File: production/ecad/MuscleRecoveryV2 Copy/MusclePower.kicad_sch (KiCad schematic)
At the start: 23 parts, among them IC1 LC709203FQH-01TWG, Q1 FDN340P, U1 AP1117-33, U2 MCP73831-2-OT

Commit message: Created New Layout
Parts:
- C15, C16, C17, C18, C5: footprint Capacitor_SMD:C_0805_2012Metric -> Capacitor_SMD:C_0402_1005Metric
- D1: footprint LED_THT:LED_D1.8mm_W3.3mm_H2.4mm -> Inductor_SMD:L_01005_0402Metric
- D3, D4: footprint LED_THT:LED_D1.8mm_W3.3mm_H2.4mm -> LED_SMD:LED_0402_1005Metric
- R32, R33, R36, R37, R38, R39: footprint Resistor_SMD:R_0805_2012Metric -> Resistor_SMD:R_0402_1005Metric
- R41, R42, R43: footprint Resistor_SMD:R_0805_2012Metric -> Resistor_SMD:R_01005_0402Metric
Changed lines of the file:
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@@
       (effects (font (size 1.27 1.27)) (justify left))
     )
-    (property "Footprint" "Capacitor_SMD:C_0805_2012Metric" (at 132.715 51.435 0)
+    (property "Footprint" "Capacitor_SMD:C_0402_1005Metric" (at 132.715 51.435 0)
       (effects (font (size 1.27 1.27)) hide)
     )
@@
       (effects (font (size 1.27 1.27)))
     )
-    (property "Footprint" "Resistor_SMD:R_0805_2012Metric" (at 149.86 49.53 0)
+    (property "Footprint" "Resistor_SMD:R_0402_1005Metric" (at 149.86 49.53 0)
       (effects (font (size 1.27 1.27)) hide)
     )
@@
       (effects (font (size 1.27 1.27)))
     )
-    (property "Footprint" "Resistor_SMD:R_0805_2012Metric" (at 64.77 114.808 90)
+    (property "Footprint" "Resistor_SMD:R_01005_0402Metric" (at 64.77 114.808 90)
       (effects (font (size 1.27 1.27)) hide)
     )
@@
       (effects (font (size 1.27 1.27)) (justify left))
     )
-    (property "Footprint" "Resistor_SMD:R_0805_2012Metric" (at 96.012 106.68 90)
+    (property "Footprint" "Resistor_SMD:R_0402_1005Metric" (at 96.012 106.68 90)
       (effects (font (size 1.27 1.27)) hide)
     )
@@
       (effects (font (size 1.27 1.27)))
     )
-    (property "Footprint" "Resistor_SMD:R_0805_2012Metric" (at 64.77 117.348 90)
+    (property "Footprint" "Resistor_SMD:R_01005_0402Metric" (at 64.77 117.348 90)
       (effects (font (size 1.27 1.27)) hide)
     )
@@
       (effects (font (size 1.27 1.27)))
     )
-    (property "Footprint" "Resistor_SMD:R_0805_2012Metric" (at 38.608 102.87 90)
+    (property "Footprint" "Resistor_SMD:R_01005_0402Metric" (at 38.608 102.87 90)
       (effects (font (size 1.27 1.27)) hide)
     )
@@
       (effects (font (size 1.27 1.27)))
     )
-    (property "Footprint" "Resistor_SMD:R_0805_2012Metric" (at 149.86 58.42 0)
+    (property "Footprint" "Resistor_SMD:R_0402_1005Metric" (at 149.86 58.42 0)
       (effects (font (size 1.27 1.27)) hide)
     )
@@
       (effects (font (size 1.27 1.27)))
     )
-    (property "Footprint" "LED_THT:LED_D1.8mm_W3.3mm_H2.4mm" (at 159.385 58.42 90)
+    (property "Footprint" "LED_SMD:LED_0402_1005Metric" (at 159.385 58.42 90)
       (effects (font (size 1.27 1.27)) hide)
     )
@@
       (effects (font (size 1.27 1.27)) (justify left))
     )
-    (property "Footprint" "Capacitor_SMD:C_0805_2012Metric" (at 23.8252 111.76 0)
+    (property "Footprint" "Capacitor_SMD:C_0402_1005Metric" (at 23.8252 111.76 0)
       (effects (font (size 1.27 1.27)) hide)
     )
@@
       (effects (font (size 1.27 1.27)) (justify left))
     )
-    (property "Footprint" "Resistor_SMD:R_0805_2012Metric" (at 41.91 118.618 90)
+    (property "Footprint" "Resistor_SMD:R_0402_1005Metric" (at 41.91 118.618 90)
       (effects (font (size 1.27 1.27)) hide)
     )
@@
       (effects (font (size 1.27 1.27)) (justify left))
     )
-    (property "Footprint" "Capacitor_SMD:C_0805_2012Metric" (at 50.8 58.42 0)
+    (property "Footprint" "Capacitor_SMD:C_0402_1005Metric" (at 50.8 58.42 0)
       (effects (font (size 1.27 1.27)) hide)
     )
@@
       (effects (font (size 1.27 1.27)) (justify right))
     )
-    (property "Footprint" "LED_THT:LED_D1.8mm_W3.3mm_H2.4mm" (at 36.83 110.49 0)
+    (property "Footprint" "Inductor_SMD:L_01005_0402Metric" (at 36.83 110.49 0)
       (effects (font (size 1.27 1.27)) hide)
     )
@@
       (effects (font (size 1.27 1.27)) (justify left))
     )
-    (property "Footprint" "Capacitor_SMD:C_0805_2012Metric" (at 95.25 58.42 0)
+    (property "Footprint" "Capacitor_SMD:C_0402_1005Metric" (at 95.25 58.42 0)
       (effects (font (size 1.27 1.27)) hide)
     )
@@
       (effects (font (size 1.27 1.27)) (justify left))
     )
-    (property "Footprint" "Capacitor_SMD:C_0805_2012Metric" (at 202.565 48.895 0)
+    (property "Footprint" "Capacitor_SMD:C_0402_1005Metric" (at 202.565 48.895 0)
       (effects (font (size 1.27 1.27)) hide)
     )
@@
       (effects (font (size 1.27 1.27)))
     )
-    (property "Footprint" "LED_THT:LED_D1.8mm_W3.3mm_H2.4mm" (at 159.385 49.53 90)
+    (property "Footprint" "LED_SMD:LED_0402_1005Metric" (at 159.385 49.53 90)
       (effects (font (size 1.27 1.27)) hide)
     )
@@
       (effects (font (size 1.27 1.27)))
     )
-    (property "Footprint" "Resistor_SMD:R_0805_2012Metric" (at 193.675 52.705 0)
+    (property "Footprint" "Resistor_SMD:R_0402_1005Metric" (at 193.675 52.705 0)
       (effects (font (size 1.27 1.27)) hide)
     )
@@
       (effects (font (size 1.27 1.27)) (justify left))
     )
-    (property "Footprint" "Resistor_SMD:R_0805_2012Metric" (at 27.94 59.69 0)
-      (effects (font (size 1.27 1.27)) hide)
-    )
+    (property "Footprint" "Resistor_SMD:R_0402_1005Metric" (at 27.94 59.69 0)
+      (effects (font (size 1.27 1.27)) hide)
+    )

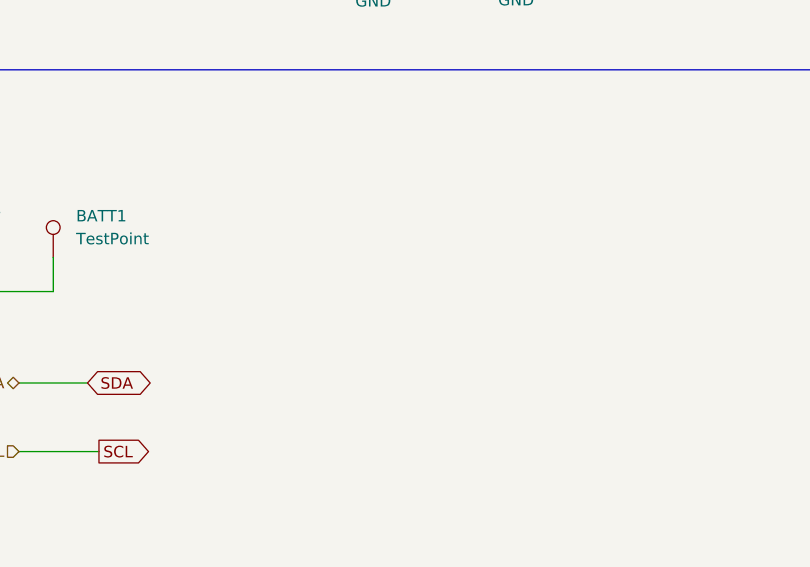
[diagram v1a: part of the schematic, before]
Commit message: Pushing Layout Changes for Andy's Layout
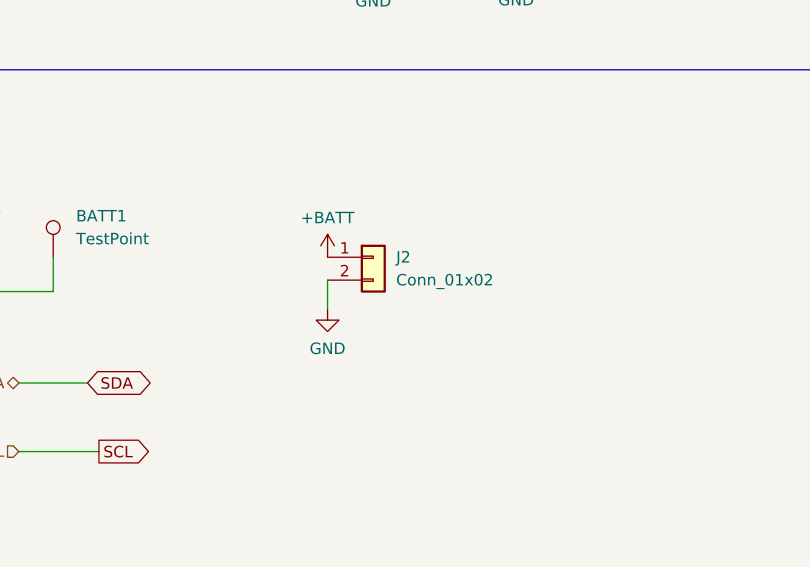
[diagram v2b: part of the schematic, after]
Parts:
- added J2: Conn_01x02, Connector:JWT_A3963_1x02_P3.96mm_Vertical, symbol Connector_Generic:Conn_01x02
- R41, R42, R43: footprint Resistor_SMD:R_01005_0402Metric -> Resistor_SMD:R_0402_1005Metric
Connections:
- net +BATT: now also J2.1 (Pin_1)
- net GND: now also J2.2 (Pin_2)
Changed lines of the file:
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@@
+    (stroke (width 0) (type default))
+  )
+  (wire (pts (xy 172.72 102.87) (xy 172.72 106.045))
     (stroke (width 0) (type default))
   )
@@
       (effects (font (size 1.27 1.27)))
     )
-    (property "Footprint" "Resistor_SMD:R_01005_0402Metric" (at 64.77 114.808 90)
+    (property "Footprint" "Resistor_SMD:R_0402_1005Metric" (at 64.77 114.808 90)
       (effects (font (size 1.27 1.27)) hide)
     )
@@
         (path "/ec7ffed6-1d2d-48f7-b073-d0a7d4b8c858"
           (reference "#PWR026") (unit 1)
+        )
+      )
+    )
+  )
+  (symbol (lib_id "power:+BATT") (at 172.72 100.33 0) (unit 1)
+    (in_bom yes) (on_board yes) (dnp no) (fields_autoplaced)
+    (property "Reference" "#PWR064" (at 172.72 104.14 0)
+      (effects (font (size 1.27 1.27)) hide)
+    )
+    (property "Value" "+BATT" (at 172.72 95.9612 0)
+      (effects (font (size 1.27 1.27)))
+    )
+    (property "Footprint" "" (at 172.72 100.33 0)
+      (effects (font (size 1.27 1.27)) hide)
+    )
+    (property "Datasheet" "" (at 172.72 100.33 0)
+      (effects (font (size 1.27 1.27)) hide)
+    )
+    (pin "1")
+    (instances
+      (project "MuscleRecoveryV1"
+        (path "/4e550305-79d2-4e4a-a502-817ebcc79f9a/648f095b-a230-48ff-8dbf-d0fbef398770"
+          (reference "#PWR064") (unit 1)
+        )
+      )
+      (project "Power For Muscle Recovery"
+        (path "/68ba6acb-d7b0-4091-ad4f-10769cda4f80"
+          (reference "#PWR02") (unit 1)
+        )
+      )
+      (project "New Test"
+        (path "/ec7ffed6-1d2d-48f7-b073-d0a7d4b8c858"
+          (reference "#PWR03") (unit 1)
         )
       )
@@
       (effects (font (size 1.27 1.27)))
     )
-    (property "Footprint" "Resistor_SMD:R_01005_0402Metric" (at 64.77 117.348 90)
+    (property "Footprint" "Resistor_SMD:R_0402_1005Metric" (at 64.77 117.348 90)
       (effects (font (size 1.27 1.27)) hide)
     )
@@
       (effects (font (size 1.27 1.27)))
     )
-    (property "Footprint" "Resistor_SMD:R_01005_0402Metric" (at 38.608 102.87 90)
+    (property "Footprint" "Resistor_SMD:R_0402_1005Metric" (at 38.608 102.87 90)
       (effects (font (size 1.27 1.27)) hide)
     )
@@
     )
   )
+  (symbol (lib_id "power:GND") (at 172.72 106.045 0) (unit 1)
+    (in_bom yes) (on_board yes) (dnp no) (fields_autoplaced)
+    (property "Reference" "#PWR065" (at 172.72 112.395 0)
+      (effects (font (size 1.27 1.27)) hide)
+    )
+    (property "Value" "GND" (at 172.72 110.49 0)
+      (effects (font (size 1.27 1.27)))
+    )
+    (property "Footprint" "" (at 172.72 106.045 0)
+      (effects (font (size 1.27 1.27)) hide)
+    )
+    (property "Datasheet" "" (at 172.72 106.045 0)
+      (effects (font (size 1.27 1.27)) hide)
+    )
+    (pin "1")
+    (instances
+      (project "MuscleRecoveryV1"
+        (path "/4e550305-79d2-4e4a-a502-817ebcc79f9a/648f095b-a230-48ff-8dbf-d0fbef398770"
+          (reference "#PWR065") (unit 1)
+        )
+      )
+    )
+  )
   (symbol (lib_id "Device:LED") (at 36.83 110.49 90) (unit 1)
     (in_bom yes) (on_board yes) (dnp no)
@@
         )
       )
+    )
+  )
+  (symbol (lib_id "Connector_Generic:Conn_01x02") (at 177.8 100.33 0) (unit 1)
+    (in_bom yes) (on_board yes) (dnp no) (fields_autoplaced)
+    (property "Reference" "J2" (at 180.34 100.33 0)
+      (effects (font (size 1.27 1.27)) (justify left))
+    )
+    (property "Value" "Conn_01x02" (at 180.34 102.87 0)
+      (effects (font (size 1.27 1.27)) (justify left))
+    )
+    (property "Footprint" "Connector:JWT_A3963_1x02_P3.96mm_Vertical" (at 177.8 100.33 0)
+      (effects (font (size 1.27 1.27)) hide)
+    )
+    (property "Datasheet" "~" (at 177.8 100.33 0)
+      (effects (font (size 1.27 1.27)) hide)
+    )
+    (pin "1")
+    (pin "2")
+    (instances
+      (project "MuscleRecoveryV1"
+        (path "/4e550305-79d2-4e4a-a502-817ebcc79f9a/648f095b-a230-48ff-8dbf-d0fbef398770"
+          (reference "J2") (unit 1)
+        )
+      )

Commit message: Committing My pliminary placement for my PCB <3
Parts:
- C15, C16: footprint Capacitor_SMD:C_0402_1005Metric -> Capacitor_SMD:C_0805_2012Metric
- R32: footprint Resistor_SMD:R_0402_1005Metric -> Resistor_SMD:R_0805_2012Metric
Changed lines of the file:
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@@
       (effects (font (size 1.27 1.27)) (justify left))
     )
-    (property "Footprint" "Capacitor_SMD:C_0402_1005Metric" (at 50.8 58.42 0)
+    (property "Footprint" "Capacitor_SMD:C_0805_2012Metric" (at 50.8 58.42 0)
       (effects (font (size 1.27 1.27)) hide)
     )
@@
       (effects (font (size 1.27 1.27)) (justify left))
     )
-    (property "Footprint" "Capacitor_SMD:C_0402_1005Metric" (at 95.25 58.42 0)
+    (property "Footprint" "Capacitor_SMD:C_0805_2012Metric" (at 95.25 58.42 0)
       (effects (font (size 1.27 1.27)) hide)
     )
@@
       (effects (font (size 1.27 1.27)) (justify left))
     )
-    (property "Footprint" "Resistor_SMD:R_0402_1005Metric" (at 27.94 59.69 0)
-      (effects (font (size 1.27 1.27)) hide)
-    )
+    (property "Footprint" "Resistor_SMD:R_0805_2012Metric" (at 27.94 59.69 0)
+      (effects (font (size 1.27 1.27)) hide)
+    )

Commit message: committing some recent changes to layout
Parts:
- removed J2: Conn_01x02, Connector:JWT_A3963_1x02_P3.96mm_Vertical, symbol Connector_Generic:Conn_01x02
- added J1: S2B-PH-SM4-TB_LF__SN_, Muscle_Recovery_Footprint_Library:JST_S2B-PH-SM4-TB_LF__SN_, symbol MuscleRecoverySymbolLibray:S2B-PH-SM4-TB_LF__SN_
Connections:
- net +BATT: now also J1.1
- net GND: now also J1.2
- no-connect marks 2 -> 4
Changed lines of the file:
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@@
   (junction (at 50.8 54.0004) (diameter 0) (color 0 0 0 0)
   )
+  (no_connect (at 184.15 104.775))
   (no_connect (at 91.44 118.11))
   (no_connect (at 91.44 120.65))
+  (no_connect (at 184.15 107.315))
   (wire (pts (xy 95.25 49.53) (xy 95.25 51.7144))
     (stroke (width 0) (type default))
@@
     (stroke (width 0) (type default))
   )
+  (wire (pts (xy 184.15 99.695) (xy 175.26 99.695))
+    (stroke (width 0) (type default))
+  )
   (wire (pts (xy 152.4 49.53) (xy 156.845 49.53))
     (stroke (width 0) (type default))
@@
     (stroke (width 0) (type default))
   )
-  (wire (pts (xy 172.72 102.87) (xy 172.72 106.045))
-    (stroke (width 0) (type default))
-  )
   (wire (pts (xy 27.94 48.26) (xy 27.94 53.848))
     (stroke (width 0) (type default))
@@
     (stroke (width 0) (type default))
   )
+  (wire (pts (xy 180.975 97.155) (xy 184.15 97.155))
+    (stroke (width 0) (type default))
+  )
   (wire (pts (xy 50.8 37.0332) (xy 50.8 43.18))
     (stroke (width 0) (type default))
@@
     (stroke (width 0) (type default))
   )
+  (wire (pts (xy 175.26 99.695) (xy 175.26 106.68))
+    (stroke (width 0) (type default))
+  )
   (wire (pts (xy 58.42 115.57) (xy 60.96 115.57))
     (stroke (width 0) (type default))
@@
   )
   (wire (pts (xy 50.8 54.0004) (xy 50.8 55.88))
+    (stroke (width 0) (type default))
+  )
+  (wire (pts (xy 180.975 95.885) (xy 180.975 97.155))
     (stroke (width 0) (type default))
   )
@@
     )
   )
-  (symbol (lib_id "power:+BATT") (at 172.72 100.33 0) (unit 1)
-    (in_bom yes) (on_board yes) (dnp no) (fields_autoplaced)
-    (property "Reference" "#PWR064" (at 172.72 104.14 0)
-      (effects (font (size 1.27 1.27)) hide)
-    )
-    (property "Value" "+BATT" (at 172.72 95.9612 0)
-      (effects (font (size 1.27 1.27)))
-    )
-    (property "Footprint" "" (at 172.72 100.33 0)
-      (effects (font (size 1.27 1.27)) hide)
-    )
-    (property "Datasheet" "" (at 172.72 100.33 0)
+  (symbol (lib_id "power:+BATT") (at 180.975 95.885 0) (unit 1)
+    (in_bom yes) (on_board yes) (dnp no) (fields_autoplaced)
+    (property "Reference" "#PWR064" (at 180.975 99.695 0)
+      (effects (font (size 1.27 1.27)) hide)
+    )
+    (property "Value" "+BATT" (at 180.975 91.5162 0)
+      (effects (font (size 1.27 1.27)))
+    )
+    (property "Footprint" "" (at 180.975 95.885 0)
+      (effects (font (size 1.27 1.27)) hide)
+    )
+    (property "Datasheet" "" (at 180.975 95.885 0)
       (effects (font (size 1.27 1.27)) hide)
     )
@@
     )
   )
-  (symbol (lib_id "power:GND") (at 172.72 106.045 0) (unit 1)
-    (in_bom yes) (on_board yes) (dnp no) (fields_autoplaced)
-    (property "Reference" "#PWR065" (at 172.72 112.395 0)
-      (effects (font (size 1.27 1.27)) hide)
-    )
-    (property "Value" "GND" (at 172.72 110.49 0)
-      (effects (font (size 1.27 1.27)))
-    )
-    (property "Footprint" "" (at 172.72 106.045 0)
-      (effects (font (size 1.27 1.27)) hide)
-    )
-    (property "Datasheet" "" (at 172.72 106.045 0)
+  (symbol (lib_id "MuscleRecoverySymbolLibray:S2B-PH-SM4-TB_LF__SN_") (at 191.77 100.965 0) (unit 1)
+    (in_bom yes) (on_board yes) (dnp no)
+    (property "Reference" "J1" (at 187.325 94.615 0)
+      (effects (font (size 1.27 1.27)) (justify left))
+    )
+    (property "Value" "S2B-PH-SM4-TB_LF__SN_" (at 186.69 110.49 0)
+      (effects (font (size 1.27 1.27)) (justify left))
+    )
+    (property "Footprint" "Muscle_Recovery_Footprint_Library:JST_S2B-PH-SM4-TB_LF__SN_" (at 193.04 118.745 0)
+      (effects (font (size 1.27 1.27)) (justify bottom) hide)
+    )
+    (property "Datasheet" "" (at 191.77 100.965 0)
+      (effects (font (size 1.27 1.27)) hide)
+    )
+    (property "MF" "JST Sales" (at 208.28 103.505 0)
+      (effects (font (size 1.27 1.27)) (justify bottom) hide)
+    )
+    (property "Description" "\nConnector Header Surface Mount, Right Angle 2 position 0.079 (2.00mm)\n" (at 191.77 122.555 0)
+      (effects (font (size 1.27 1.27)) (justify bottom) hide)
+    )
+    (property "Package" "None" (at 212.09 99.695 0)
+      (effects (font (size 1.27 1.27)) (justify bottom) hide)
+    )
+    (property "Price" "None" (at 191.77 100.965 0)
+      (effects (font (size 1.27 1.27)) (justify bottom) hide)
+    )
+    (property "Check_prices" "https://www.snapeda.com/parts/S2B-PH-SM4-TB(LF)(SN)/JST+Sales+America+Inc./view-part/?ref=eda" (at 190.5 118.745 0)
+      (effects (font (size 1.27 1.27)) (justify bottom) hide)
+    )
+    (property "STANDARD" "Manufacturer Recommendation" (at 193.04 123.825 0)
+      (effects (font (size 1.27 1.27)) (justify bottom) hide)
+    )
+    (property "SnapEDA_Link" "https://www.snapeda.com/parts/S2B-PH-SM4-TB(LF)(SN)/JST+Sales+America+Inc./view-part/?ref=snap" (at 194.31 120.015 0)
+      (effects (font (size 1.27 1.27)) (justify bottom) hide)
+    )
+    (property "MP" "S2B-PH-SM4-TB(LF)(SN)" (at 191.77 114.935 0)
+      (effects (font (size 1.27 1.27)) (justify bottom) hide)
+    )
+    (property "Availability" "In Stock" (at 212.09 109.855 0)
+      (effects (font (size 1.27 1.27)) (justify bottom) hide)
+    )
+    (property "MANUFACTURER" "JST" (at 207.01 98.425 0)
+      (effects (font (size 1.27 1.27)) (justify bottom) hide)
+    )
+    (pin "1")
+    (pin "2")
+    (pin "S1")
+    (pin "S2")
+    (instances
+      (project "MuscleRecoveryV1"
+        (path "/4e550305-79d2-4e4a-a502-817ebcc79f9a/648f095b-a230-48ff-8dbf-d0fbef398770"
+          (reference "J1") (unit 1)
+        )
+      )
+    )
+  )
+  (symbol (lib_id "power:GND") (at 175.26 106.68 0) (unit 1)
+    (in_bom yes) (on_board yes) (dnp no) (fields_autoplaced)
+    (property "Reference" "#PWR065" (at 175.26 113.03 0)
+      (effects (font (size 1.27 1.27)) hide)
+    )
+    (property "Value" "GND" (at 175.26 111.125 0)
+      (effects (font (size 1.27 1.27)))
+    )
+    (property "Footprint" "" (at 175.26 106.68 0)
+      (effects (font (size 1.27 1.27)) hide)
+    )
+    (property "Datasheet" "" (at 175.26 106.68 0)
       (effects (font (size 1.27 1.27)) hide)
     )
@@
         )
       )
-    )
-  )
-  (symbol (lib_id "Connector_Generic:Conn_01x02") (at 177.8 100.33 0) (unit 1)
-    (in_bom yes) (on_board yes) (dnp no) (fields_autoplaced)
-    (property "Reference" "J2" (at 180.34 100.33 0)
-      (effects (font (size 1.27 1.27)) (justify left))
-    )
-    (property "Value" "Conn_01x02" (at 180.34 102.87 0)
-      (effects (font (size 1.27 1.27)) (justify left))
-    )
-    (property "Footprint" "Connector:JWT_A3963_1x02_P3.96mm_Vertical" (at 177.8 100.33 0)
-      (effects (font (size 1.27 1.27)) hide)
-    )
-    (property "Datasheet" "~" (at 177.8 100.33 0)
-      (effects (font (size 1.27 1.27)) hide)
-    )
-    (pin "1")
-    (pin "2")
-    (instances
-      (project "MuscleRecoveryV1"
-        (path "/4e550305-79d2-4e4a-a502-817ebcc79f9a/648f095b-a230-48ff-8dbf-d0fbef398770"
-          (reference "J2") (unit 1)
-        )
-      )

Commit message: Pushing Most of the final changes for PCB REV2
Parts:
- removed BATT1: TestPoint, TestPoint:TestPoint_Pad_D1.5mm, symbol Connector:TestPoint
- removed D1: GREEN, Inductor_SMD:L_01005_0402Metric, symbol Device:LED
- removed IC1: LC709203FQH-01TWG, Package_DFN_QFN:WDFN-8-1EP_4x3mm_P0.65mm_EP2.4x1.8mm, symbol Battery_Management:LC709203FQH-01TWG
- removed R36, R37: 10K, Resistor_SMD:R_0402_1005Metric, symbol Device:R
- removed R41, R42, R43: 0, Resistor_SMD:R_0402_1005Metric, symbol Device:R
- added R34: 100, Resistor_SMD:R_0402_1005Metric, symbol Device:R_Small
- added R37: 1k, Resistor_SMD:R_0402_1005Metric, symbol Device:R_Small
- added U9: MAX17043G+T, Muscle_Recovery_Footprint_Library:21-0174B_MXM-L, symbol MuscleRecoverySymbolLibray:MAX17043G+T
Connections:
- net +BATT: now also R34.1, R37.1
- net GND: now also U9.1 (CTG), U9.4 (GND), U9.9 (EPAD)
- net SCL: now also U9.7 (SCL)
- net SDA: now also U9.8 (SDA)
- net +3.3V renamed +3V3
- new net: R37.2, U9.2 (CELL)
- new net: R34.2, U9.3 (VDD)

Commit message: Pushing changes post schematic review
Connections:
- net GND: now also U9.6 (QSRT)
- no-connect marks 4 -> 3
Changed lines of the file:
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@@
   (no_connect (at 97.79 111.125))
   (no_connect (at 184.15 107.315))
-  (no_connect (at 97.79 108.585))
   (wire (pts (xy 95.25 49.53) (xy 95.25 51.7144))
     (stroke (width 0) (type default))
@@
   )
   (wire (pts (xy 78.486 59.3344) (xy 78.486 65.9384))
+    (stroke (width 0) (type default))
+  )
+  (wire (pts (xy 97.79 108.585) (xy 102.235 108.585))
     (stroke (width 0) (type default))
   )
@@
   )
   (wire (pts (xy 50.8 53.34) (xy 50.8 53.848))
+    (stroke (width 0) (type default))
+  )
+  (wire (pts (xy 102.235 108.585) (xy 102.235 118.745))
     (stroke (width 0) (type default))
   )
@@
         )
       )
+    )
+  )
+  (symbol (lib_id "power:GND") (at 102.235 118.745 0) (unit 1)
+    (in_bom yes) (on_board yes) (dnp no) (fields_autoplaced)
+    (property "Reference" "#PWR01" (at 102.235 125.095 0)
+      (effects (font (size 1.27 1.27)) hide)
+    )
+    (property "Value" "GND" (at 102.235 123.825 0)
+      (effects (font (size 1.27 1.27)))
+    )
+    (property "Footprint" "" (at 102.235 118.745 0)
+      (effects (font (size 1.27 1.27)) hide)
+    )
+    (property "Datasheet" "" (at 102.235 118.745 0)
+      (effects (font (size 1.27 1.27)) hide)
+    )
+    (pin "1")
+    (instances
+      (project "MuscleRecoveryV1"
+        (path "/4e550305-79d2-4e4a-a502-817ebcc79f9a/648f095b-a230-48ff-8dbf-d0fbef398770"
+          (reference "#PWR01") (unit 1)
+        )
+      )

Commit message: Pushing final Rev2 PCBA Files
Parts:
- added TP1, TP2, TP3, TP4, TP5, TP8, TP9: TestPoint, TestPoint:TestPoint_Pad_1.0x1.0mm, symbol Connector:TestPoint
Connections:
- net +3V3: now also TP3.1
- net +BATT: now also TP2.1
- net GND: now also TP8.1, TP9.1
- net SCL: now also TP5.1
- net SDA: now also TP4.1
- net VBUS: now also TP1.1
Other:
- moved on the sheet: C5
